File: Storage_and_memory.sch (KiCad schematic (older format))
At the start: 10 parts, among them J4 DM3AT-SF-PEJM5, U14 TXS0206-29YFPRB, U15 W25Q256JVFIQ

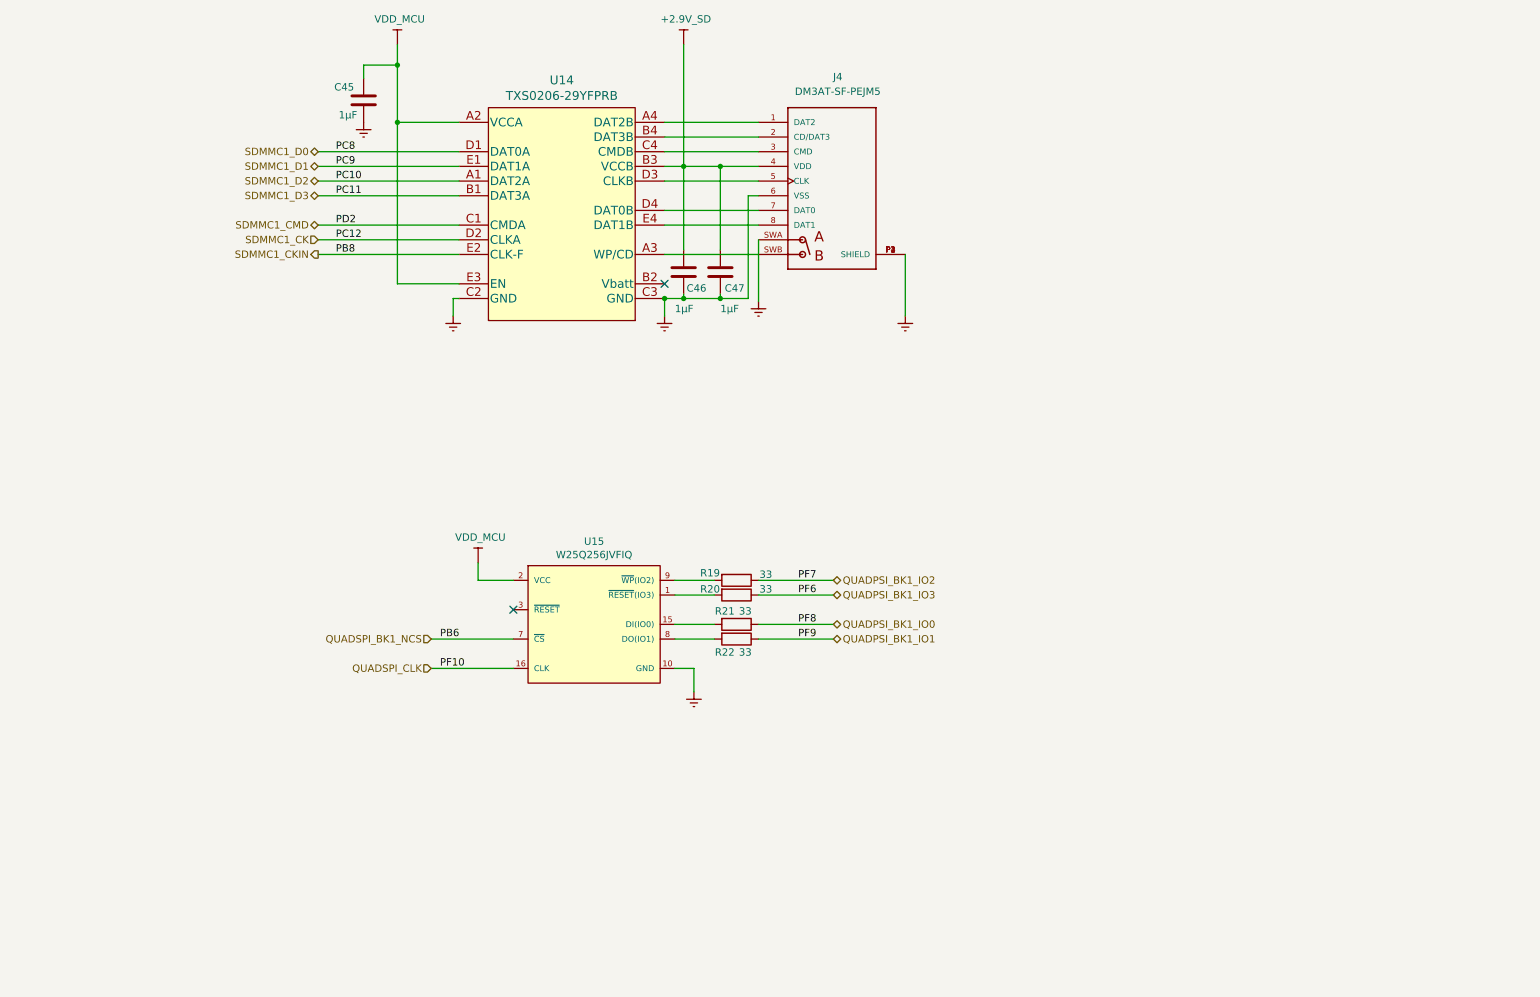
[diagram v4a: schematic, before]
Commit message: deleted TXS0206 added SN74AVCA406DGGR and corrected schema for it
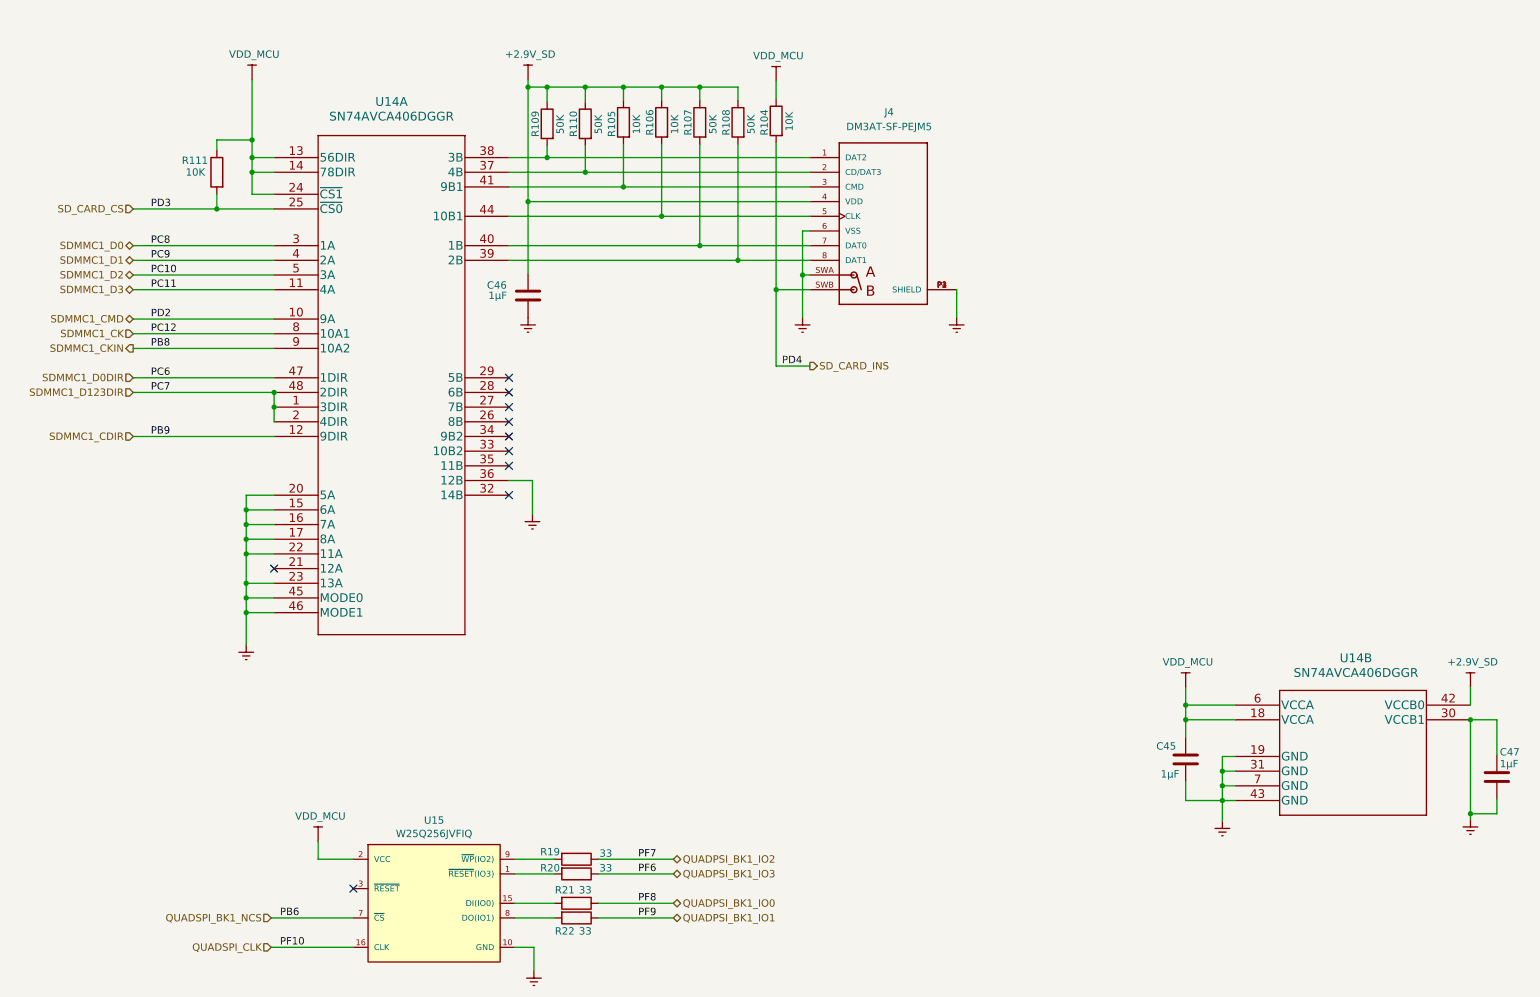
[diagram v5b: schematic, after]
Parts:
- removed U14: TXS0206-29YFPRB, SVIELCOM:TXS0206-29YFPRB, symbol SVIELCOM_Library:TXS0206-29YFPRB
- added R104, R105, R106, R111: 10K, Resistor_SMD:R_0805_2012Metric_Pad1.20x1.40mm_HandSolder, symbol Device:R
- added R107, R108, R109, R110: 50K, Resistor_SMD:R_0805_2012Metric_Pad1.20x1.40mm_HandSolder, symbol Device:R
- added U14: SN74AVCA406DGGR, SVIELCOM:SN74AVCA406DGGR, symbol SVIELCOM_Library:SN74AVCA406DGGR
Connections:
- net +2,9V: now also R105.1, R106.1, R107.1, R108.1, R109.1, R110.1, U14.42 (VCCB0); no longer C47.1
- net GNDREF: now also C47.1, U14.15 (6A), U14.16 (7A), U14.17 (8A), U14.19 (GND), U14.20 (5A), U14.22 (11A), U14.23 (13A), U14.30 (VCCB1), U14.31 (GND), U14.36 (12B), U14.43 (GND), U14.45 (MODE0), U14.46 (MODE1), U14.7 (GND)
- net SDMMC1_CK: now also U14.8 (10A1)
- net SDMMC1_CKIN: now also U14.9 (10A2)
- net SDMMC1_CMD: now also U14.10 (9A)
- net SDMMC1_D0: now also U14.3 (1A)
- net SDMMC1_D1: now also U14.4 (2A)
- net SDMMC1_D2: now also U14.5 (3A)
- net SDMMC1_D3: now also U14.11 (4A)
- net VDD_MCU: now also R104.1, R111.1, U14.13 (56DIR), U14.14 (78DIR), U14.18 (VCCA), U14.24 (~CS1), U14.6 (VCCA)
- net SD_CARD_INS: now reaches J4.SWB
- net SD_CARD_INS: now also R104.2
- net at J4.1 (DAT2): now also R109.2, U14.38 (3B)
- net at J4.2 (CD/DAT3): now also R110.2, U14.37 (4B)
- net at J4.3 (CMD): now also R105.2, U14.41 (9B1)
- net at J4.5 (CLK): now also R106.2, U14.44 (10B1)
- net at J4.7 (DAT0): now also R107.2, U14.40 (1B)
- net at J4.8 (DAT1): now also R108.2, U14.39 (2B)
- new net SDMMC1_CDIR: U14.12 (9DIR)
- new net SDMMC1_D0DIR: U14.47 (1DIR)
- new net SDMMC1_D123DIR: U14.1 (3DIR), U14.2 (4DIR), U14.48 (2DIR)
- new net SD_CARD_CS: R111.2, U14.25 (~CS0)
- no-connect marks 2 -> 10
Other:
- moved on the sheet: C45, C46, C47, J4, R19, R20, R21, R22, U15

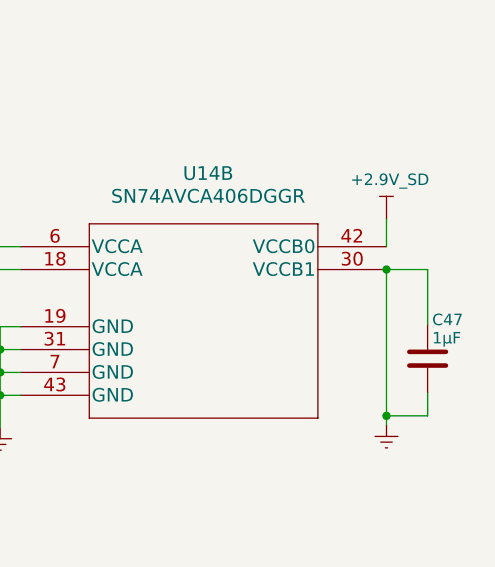
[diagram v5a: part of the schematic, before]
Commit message: LAN elements placed
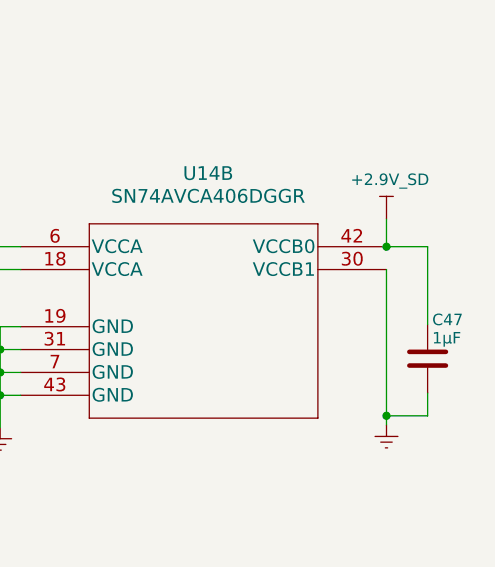
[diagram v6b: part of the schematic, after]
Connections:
- net +2,9V: now also C47.1
- net GNDREF: no longer C47.1
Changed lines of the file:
@@
 Wire Wire Line
 	10790 6300 10790 6340
-Wire Wire Line
-	10970 5900 10970 5660
-Wire Wire Line
-	10970 5660 10790 5660
-Connection ~ 10790 5660
 $Comp
 L SVIELCOM_Library:+2.9V_SD #PWR0127
@@
 Wire Wire Line
 	4400 4030 4400 4260
+Wire Wire Line
+	10790 5560 10970 5560
+Wire Wire Line
+	10970 5560 10970 5900
+Connection ~ 10790 5560
 $EndSCHEMATC

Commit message: PCB before Gerber creating
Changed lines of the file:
@@
 SD_CARD_CS
 Text Label 1800 2180 0    50   ~ 0
+PD4
+Text Label 6100 3250 0    50   ~ 0
 PD3
-Text Label 6100 3250 0    50   ~ 0
-PD4
 $Comp
 L Device:R R?

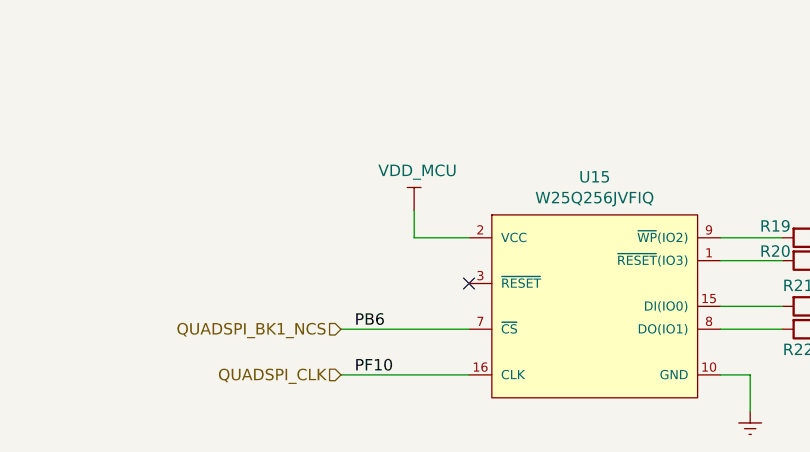
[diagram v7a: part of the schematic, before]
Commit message: minor changes and add NRST to J16
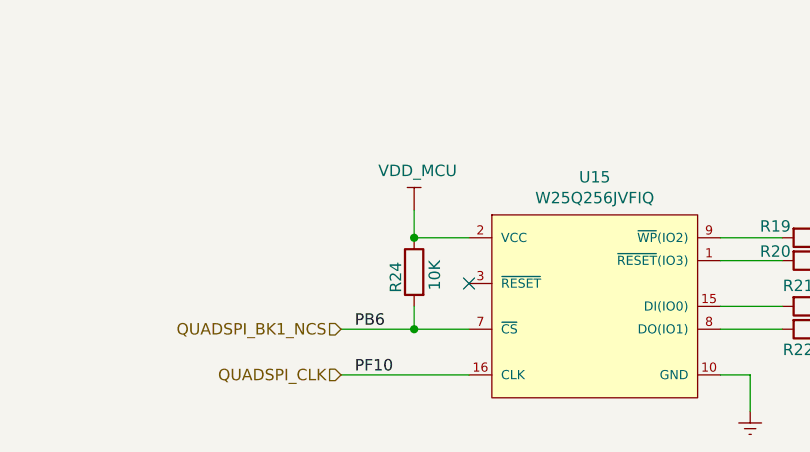
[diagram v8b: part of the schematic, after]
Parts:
- added R24: 10K, Resistor_SMD:R_0805_2012Metric_Pad1.20x1.40mm_HandSolder, symbol Device:R
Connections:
- net QUADSPI_BK1_NCS: now also R24.2
- net VDD_MCU: now also R24.1
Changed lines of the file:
@@
 NoConn ~ 3180 6810
 Wire Wire Line
-	2620 7010 3180 7010
+	2620 7010 2940 7010
 Wire Wire Line
 	2620 7210 3180 7210
@@
 	10970 5560 10970 5900
 Connection ~ 10790 5560
+$Comp
+L Device:R R?
+U 1 1 60C3CFB3
+P 2940 6760
+AR Path="/608C7842/60C3CFB3" Ref="R?"  Part="1"
+AR Path="/60D8A641/60C3CFB3" Ref="R24"  Part="1"
+F 0 "R24" V 3020 6670 50  0000 L CNN
+F 1 "10K" V 2850 6680 50  0000 L CNN
+F 2 "Resistor_SMD:R_0805_2012Metric_Pad1.20x1.40mm_HandSolder" V 2870 6760 50  0001 C CNN
+F 3 "~" H 2940 6760 50  0001 C CNN
+F 4 "RC0805FR-0710KL" H 2940 6760 50  0001 C CNN "Type"
+	1    2940 6760
+	-1   0    0    -1
+$EndComp
+Connection ~ 2940 6610
+Wire Wire Line
+	2940 6910 2940 7010
+Connection ~ 2940 7010
+Wire Wire Line
+	2940 7010 3180 7010
 $EndSCHEMATC
